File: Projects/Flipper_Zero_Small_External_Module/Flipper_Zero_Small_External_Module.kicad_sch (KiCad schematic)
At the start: 1 part, among them J1 Flipper_Zero

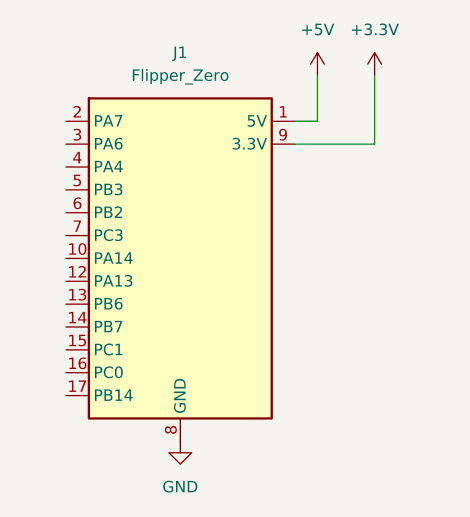
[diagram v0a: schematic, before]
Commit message: Update to KiCAD 10
Signed-off-by: Ilias Daradimos <judgedrid@gmail.com>
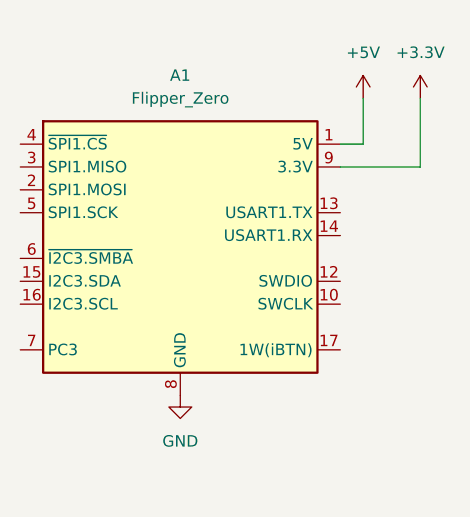
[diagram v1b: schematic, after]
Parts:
- renumbered J1 to A1
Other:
- moved on the sheet: A1
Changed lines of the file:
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@@
 (kicad_sch
-	(version 20231120)
+	(version 20260306)
 	(generator "eeschema")
-	(generator_version "8.0")
+	(generator_version "10.0")
 	(paper "A4")
 	(wire
 		(pts
-			(xy 157.48 69.85) (xy 157.48 74.93)
+			(xy 162.56 72.39) (xy 162.56 77.47)
 		)
 		(stroke
@@
 	(wire
 		(pts
-			(xy 157.48 74.93) (xy 154.94 74.93)
+			(xy 162.56 77.47) (xy 160.02 77.47)
 		)
 		(stroke
@@
 	(wire
 		(pts
-			(xy 163.83 77.47) (xy 163.83 69.85)
+			(xy 168.91 80.01) (xy 168.91 72.39)
 		)
 		(stroke
@@
 	(wire
 		(pts
-			(xy 154.94 77.47) (xy 163.83 77.47)
+			(xy 160.02 80.01) (xy 168.91 80.01)
 		)
 		(stroke
@@
 		(at 142.24 90.17 0)
 		(unit 1)
+		(body_style 1)
 		(exclude_from_sim no)
 		(in_bom yes)
 		(on_board yes)
+		(in_pos_files yes)
 		(dnp no)
 		(fields_autoplaced yes)
-		(property "Reference" "J1"
-			(at 142.24 67.31 0)
+		(property "Reference" "A1"
+			(at 142.24 69.85 0)
+			(show_name no)
+			(do_not_autoplace no)
 			(effects
 				(font
@@
 		)
 		(property "Value" "Flipper_Zero"
-			(at 142.24 69.85 0)
+			(at 142.24 72.39 0)
+			(show_name no)
+			(do_not_autoplace no)
 			(effects
 				(font
@@
 		)
 		(property "Footprint" "Module:Flipper_Zero_Straight"
-			(at 128.27 76.2 0)
-			(effects
-				(font
-					(size 1.27 1.27)
-				)
-				(hide yes)
+			(at 142.24 115.824 0)
+			(hide yes)
+			(show_name no)
+			(do_not_autoplace no)
+			(effects
+				(font
+					(size 1.27 1.27)
+				)
 			)
 		)
 		(property "Datasheet" "https://docs.flipper.net/development"
-			(at 143.256 67.564 0)
-			(effects
-				(font
-					(size 1.27 1.27)
-				)
-				(hide yes)
-			)
-		)
-		(property "Description" "Flipper Zero is a portable multi-tool for pentesters and geeks in a toy-like body"
-			(at 138.176 111.252 0)
-			(effects
-				(font
-					(size 1.27 1.27)
-				)
-				(hide yes)
+			(at 142.24 113.538 0)
+			(hide yes)
+			(show_name no)
+			(do_not_autoplace no)
+			(effects
+				(font
+					(size 1.27 1.27)
+				)
+			)
+		)
+		(property "Description" "Portable multi-tool for pentesters and geeks in a toy-like body, 13 GPIO, USB to UART/SPI/I2C bridge/converter, Serial Wire Debug interface (SWD), 2.54 mm pin header connector"
+			(at 142.24 111.252 0)
+			(hide yes)
+			(show_name no)
+			(do_not_autoplace no)
+			(effects
+				(font
+					(size 1.27 1.27)
+				)
 			)
 		)
@@
 		)
 		(instances
-			(project ""
+			(project "Flipper_Zero_Small_External_Module"
 				(path "/c67f828b-18a5-4dea-9022-e222a7d410ef"
-					(reference "J1")
+					(reference "A1")
 					(unit 1)
 				)
@@
 	(symbol
 		(lib_id "power:GND")
-		(at 142.24 110.49 0)
+		(at 142.24 105.41 0)
 		(unit 1)
+		(body_style 1)
 		(exclude_from_sim no)
 		(in_bom yes)
 		(on_board yes)
+		(in_pos_files yes)
 		(dnp no)
 		(fields_autoplaced yes)
 		(property "Reference" "#PWR01"
-			(at 142.24 116.84 0)
-			(effects
-				(font
-					(size 1.27 1.27)
-				)
-				(hide yes)
+			(at 142.24 111.76 0)
+			(hide yes)
+			(show_name no)
+			(do_not_autoplace no)
+			(effects
+				(font
+					(size 1.27 1.27)
+				)
 			)
 		)
 		(property "Value" "GND"
-			(at 142.24 115.57 0)
+			(at 142.24 110.49 0)
+			(show_name no)
+			(do_not_autoplace no)
 			(effects
 				(font
@@
 		)
 		(property "Footprint" ""
-			(at 142.24 110.49 0)
-			(effects
-				(font
-					(size 1.27 1.27)
-				)
-				(hide yes)
+			(at 142.24 105.41 0)
+			(hide yes)
+			(show_name no)
+			(do_not_autoplace no)
+			(effects
+				(font
+					(size 1.27 1.27)
+				)
 			)
 		)
 		(property "Datasheet" ""
-			(at 142.24 110.49 0)
-			(effects
-				(font
-					(size 1.27 1.27)
-				)
-				(hide yes)
+			(at 142.24 105.41 0)
+			(hide yes)
+			(show_name no)
+			(do_not_autoplace no)
+			(effects
+				(font
+					(size 1.27 1.27)
+				)
 			)
 		)
 		(property "Description" "Power symbol creates a global label with name \"GND\" , ground"
-			(at 142.24 110.49 0)
-			(effects
-				(font
-					(size 1.27 1.27)
-				)
-				(hide yes)
+			(at 142.24 105.41 0)
+			(hide yes)
+			(show_name no)
+			(do_not_autoplace no)
+			(effects
+				(font
+					(size 1.27 1.27)
+				)
 			)
 		)
@@
 		)
 		(instances
-			(project ""
+			(project "Flipper_Zero_Small_External_Module"
 				(path "/c67f828b-18a5-4dea-9022-e222a7d410ef"
 					(reference "#PWR01")
@@
 	(symbol
 		(lib_id "power:+3.3V")
-		(at 163.83 69.85 0)
+		(at 168.91 72.39 0)
 		(unit 1)
+		(body_style 1)
 		(exclude_from_sim no)
 		(in_bom yes)
 		(on_board yes)
+		(in_pos_files yes)
 		(dnp no)
 		(fields_autoplaced yes)
 		(property "Reference" "#PWR03"
-			(at 163.83 73.66 0)
-			(effects
-				(font
-					(size 1.27 1.27)
-				)
-				(hide yes)
+			(at 168.91 76.2 0)
+			(hide yes)
+			(show_name no)
+			(do_not_autoplace no)
+			(effects
+				(font
+					(size 1.27 1.27)
+				)
 			)
 		)
 		(property "Value" "+3.3V"
-			(at 163.83 64.77 0)
+			(at 168.91 67.31 0)
+			(show_name no)
+			(do_not_autoplace no)
 			(effects
 				(font
@@
 		)
 		(property "Footprint" ""
-			(at 163.83 69.85 0)
-			(effects
-				(font
-					(size 1.27 1.27)
-				)
-				(hide yes)
+			(at 168.91 72.39 0)
+			(hide yes)
+			(show_name no)
+			(do_not_autoplace no)
+			(effects
+				(font
+					(size 1.27 1.27)
+				)
 			)
 		)
 		(property "Datasheet" ""
-			(at 163.83 69.85 0)
-			(effects
-				(font
-					(size 1.27 1.27)
-				)
-				(hide yes)
+			(at 168.91 72.39 0)
+			(hide yes)
+			(show_name no)
+			(do_not_autoplace no)
+			(effects
+				(font
+					(size 1.27 1.27)
+				)
 			)
 		)
 		(property "Description" "Power symbol creates a global label with name \"+3.3V\""
-			(at 163.83 69.85 0)
-			(effects
-				(font
-					(size 1.27 1.27)
-				)
-				(hide yes)
+			(at 168.91 72.39 0)
+			(hide yes)
+			(show_name no)
+			(do_not_autoplace no)
+			(effects
+				(font
+					(size 1.27 1.27)
+				)
 			)
 		)
@@
 		)
 		(instances
-			(project ""
+			(project "Flipper_Zero_Small_External_Module"
 				(path "/c67f828b-18a5-4dea-9022-e222a7d410ef"
 					(reference "#PWR03")
@@
 	(symbol
 		(lib_id "power:+5V")
-		(at 157.48 69.85 0)
+		(at 162.56 72.39 0)
 		(unit 1)
+		(body_style 1)
 		(exclude_from_sim no)
 		(in_bom yes)
 		(on_board yes)
+		(in_pos_files yes)
 		(dnp no)
 		(fields_autoplaced yes)
 		(property "Reference" "#PWR02"
-			(at 157.48 73.66 0)
-			(effects
-				(font
-					(size 1.27 1.27)
-				)
-				(hide yes)
+			(at 162.56 76.2 0)
+			(hide yes)
+			(show_name no)
+			(do_not_autoplace no)
+			(effects
+				(font
+					(size 1.27 1.27)
+				)
 			)
 		)
 		(property "Value" "+5V"
-			(at 157.48 64.77 0)
+			(at 162.56 67.31 0)
+			(show_name no)
+			(do_not_autoplace no)
 			(effects
 				(font
@@
 		)
 		(property "Footprint" ""
-			(at 157.48 69.85 0)
-			(effects
-				(font
-					(size 1.27 1.27)
-				)
-				(hide yes)
+			(at 162.56 72.39 0)
+			(hide yes)
+			(show_name no)
+			(do_not_autoplace no)
+			(effects
+				(font
+					(size 1.27 1.27)
+				)
 			)
 		)
 		(property "Datasheet" ""
-			(at 157.48 69.85 0)
-			(effects
-				(font
-					(size 1.27 1.27)
-				)
-				(hide yes)
+			(at 162.56 72.39 0)
+			(hide yes)
+			(show_name no)
+			(do_not_autoplace no)
+			(effects
+				(font
+					(size 1.27 1.27)
+				)
 			)
 		)
 		(property "Description" "Power symbol creates a global label with name \"+5V\""
-			(at 157.48 69.85 0)
-			(effects
-				(font
-					(size 1.27 1.27)
-				)
-				(hide yes)
+			(at 162.56 72.39 0)
+			(hide yes)
+			(show_name no)
+			(do_not_autoplace no)
+			(effects
+				(font
+					(size 1.27 1.27)
+				)
 			)
 		)
@@
 		)
 		(instances
-			(project ""
+			(project "Flipper_Zero_Small_External_Module"
 				(path "/c67f828b-18a5-4dea-9022-e222a7d410ef"
 					(reference "#PWR02")
@@
 		)
 	)
+	(embedded_fonts no)
 )
